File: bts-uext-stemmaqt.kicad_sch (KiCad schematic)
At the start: 2 parts, among them J2 Conn_01x04, J3 UEXT_Slave

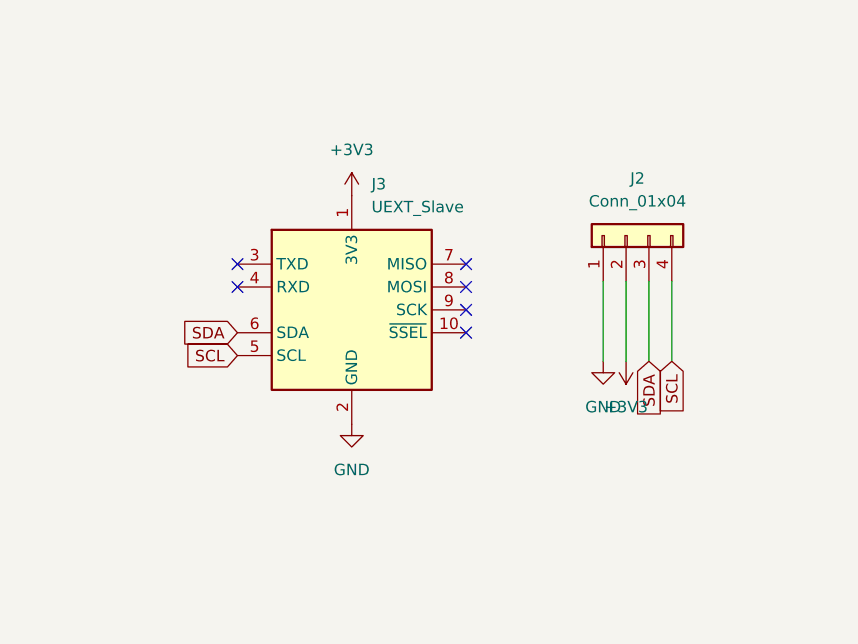
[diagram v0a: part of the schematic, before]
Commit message: Rev2: Switch 2x5 to through hole.
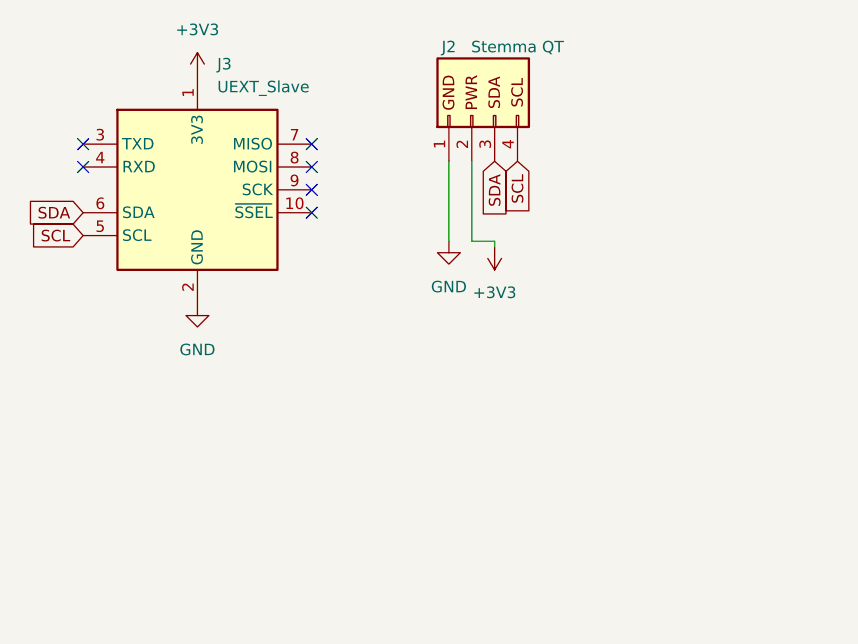
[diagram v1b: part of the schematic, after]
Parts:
- J2: value Conn_01x04 -> Stemma QT; symbol Connector_Generic:Conn_01x04 -> BTS_UEXT_STEMMA:Stemma/QT/Qwiic
- J3: footprint Connector_PinHeader_2.54mm:PinHeader_2x05_P2.54mm_Vertical_SMD -> Connector_PinHeader_2.54mm:PinHeader_2x05_P2.54mm_Vertical; LCSC C843271 -> C92270
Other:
- moved on the sheet: J3
